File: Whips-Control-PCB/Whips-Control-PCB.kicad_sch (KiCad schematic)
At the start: 6 parts, among them J1 PWR, J2 DATA, U1 Teensy4.1_Minimal, U2 MAX485E, U3 TSOP341xx

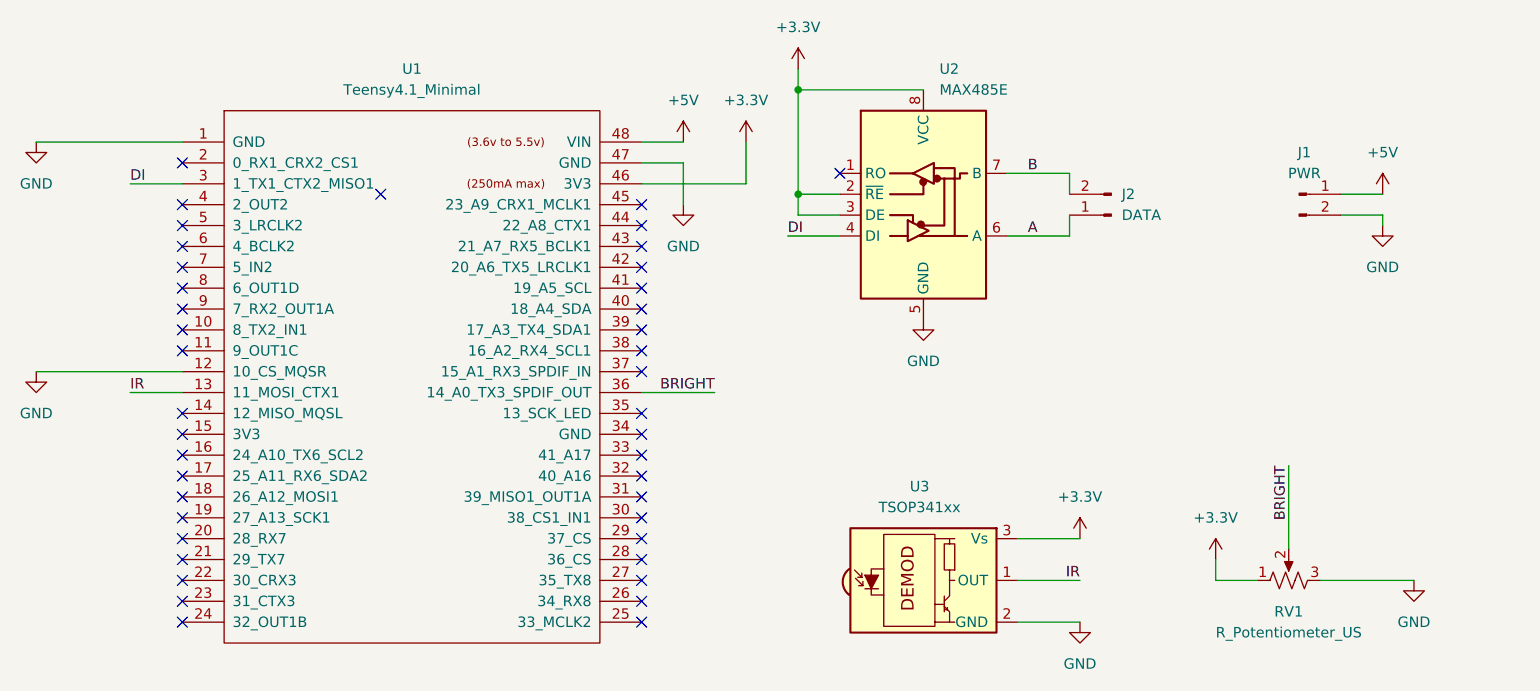
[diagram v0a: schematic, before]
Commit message: this is a new PCB for the controller, to fit in a smaller box
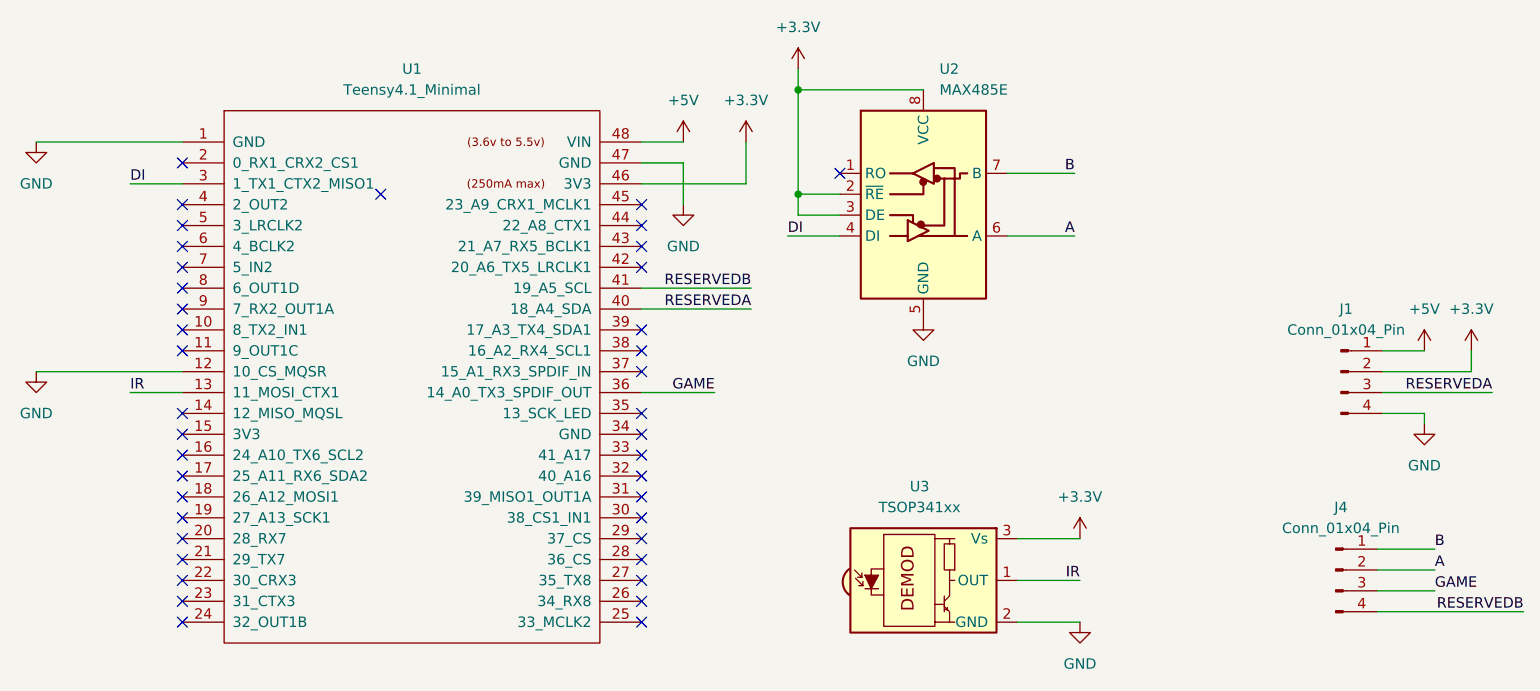
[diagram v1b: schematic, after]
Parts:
- removed J1: PWR, Connector_Phoenix_MSTB:PhoenixContact_MSTBA_2,5_2-G-5,08_1x02_P5.08mm_Horizontal, symbol Connector:Conn_01x02_Pin
- removed J2: DATA, Connector_Phoenix_MSTB:PhoenixContact_MSTBA_2,5_2-G-5,08_1x02_P5.08mm_Horizontal, symbol Connector:Conn_01x02_Pin
- removed RV1: R_Potentiometer_US, Potentiometer_THT:Potentiometer_Alpha_RD901F-40-00D_Single_Vertical, symbol Device:R_Potentiometer_US
- added J1, J4: Conn_01x04_Pin, TerminalBlock_Phoenix:TerminalBlock_Phoenix_MKDS-1,5-4_1x04_P5.00mm_Horizontal, symbol Connector:Conn_01x04_Pin
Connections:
- net +3.3V: now also J1.2 (Pin_2)
- net +5V: now also J1.1 (Pin_1)
- net A: now also J4.2 (Pin_2)
- net B: now also J4.1 (Pin_1)
- net GND: now also J1.4 (Pin_4)
- net RESERVEDA: now reaches U1.40 (18_A4_SDA)
- net RESERVEDA: now also J1.3 (Pin_3)
- net RESERVEDB: now reaches U1.41 (19_A5_SCL)
- net RESERVEDB: now also J4.4 (Pin_4)
- net BRIGHT renamed GAME
- net GAME: now also J4.3 (Pin_3)
- no-connect marks 42 -> 40
